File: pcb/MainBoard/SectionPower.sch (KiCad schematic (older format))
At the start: 14 parts, among them P3 Motor controller, P4 Motor battery, P5 Steering connector, P6 Arduino battery, SW1 OnOffDoubleSwitch

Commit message: PCB design finished
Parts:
- removed C_PWR_2, C_PWR_4: C, Capacitors_ThroughHole:C_Radial_D6.3_L11.2_P2.5, symbol C
- renumbered C_PWR_3 to C_PWR_2
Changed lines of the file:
@@
 NoConn ~ 3100 4000
 $Comp
-L GND #PWR044
+L GND #PWR042
 U 1 1 57FA5F2E
 P 5950 4950
-F 0 "#PWR044" H 5950 4700 50  0001 C CNN
+F 0 "#PWR042" H 5950 4700 50  0001 C CNN
 F 1 "GND" H 5950 4800 50  0000 C CNN
 F 2 "" H 5950 4950 50  0000 C CNN
@@
 MOTOR_B2
 $Comp
-L +5V #PWR045
+L +5V #PWR043
 U 1 1 57FA637B
 P 5950 4750
-F 0 "#PWR045" H 5950 4600 50  0001 C CNN
+F 0 "#PWR043" H 5950 4600 50  0001 C CNN
 F 1 "+5V" H 5950 4890 50  0000 C CNN
 F 2 "" H 5950 4750 50  0000 C CNN
@@
 $EndComp
 $Comp
-L C C_PWR_3
+L C C_PWR_2
 U 1 1 57FA6C6F
 P 3800 4800
-F 0 "C_PWR_3" H 3825 4900 50  0000 L CNN
+F 0 "C_PWR_2" H 3825 4900 50  0000 L CNN
 F 1 "C" H 3825 4700 50  0000 L CNN
 F 2 "Capacitors_ThroughHole:C_Radial_D6.3_L11.2_P2.5" H 3838 4650 50  0001 C CNN
@@
 	1    0    0    -1
 $EndComp
-$Comp
-L C C_PWR_4
-U 1 1 57FA6CEF
-P 4250 4800
-F 0 "C_PWR_4" H 4275 4900 50  0000 L CNN
-F 1 "C" H 4275 4700 50  0000 L CNN
-F 2 "Capacitors_ThroughHole:C_Radial_D6.3_L11.2_P2.5" H 4288 4650 50  0001 C CNN
-F 3 "" H 4250 4800 50  0000 C CNN
-	1    4250 4800
-	1    0    0    -1
-$EndComp
 Wire Wire Line
 	1900 4950 5050 4950
 Connection ~ 3800 4950
-Connection ~ 4250 4950
 Wire Wire Line
 	3500 4000 3500 4650
@@
 Wire Wire Line
 	5050 4650 5050 4750
-Connection ~ 4250 4650
-$Comp
-L C C_PWR_2
-U 1 1 57FA7057
-P 4200 2300
-F 0 "C_PWR_2" H 4225 2400 50  0000 L CNN
-F 1 "C" H 4225 2200 50  0000 L CNN
-F 2 "Capacitors_ThroughHole:C_Radial_D6.3_L11.2_P2.5" H 4238 2150 50  0001 C CNN
-F 3 "" H 4200 2300 50  0000 C CNN
-	1    4200 2300
-	1    0    0    -1
-$EndComp
 Wire Wire Line
 	3500 2150 5050 2150
 Connection ~ 3700 2150
-Connection ~ 4200 2150
 Wire Wire Line
 	1900 2450 5050 2450
@@
 Wire Wire Line
 	4650 2450 4650 3450
-Connection ~ 4200 2450
 Connection ~ 4650 2450
 Wire Wire Line

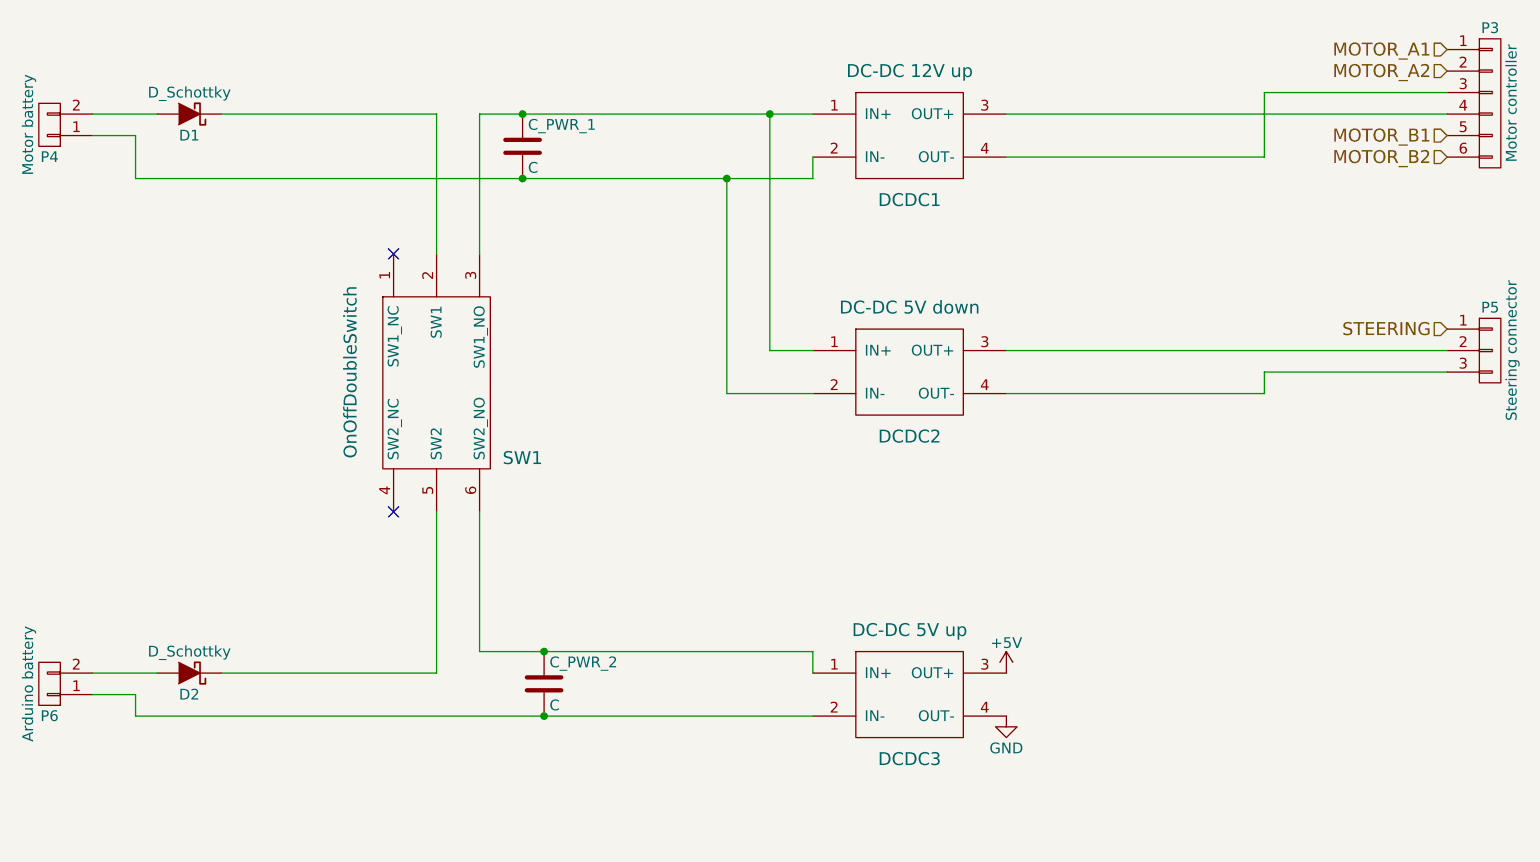
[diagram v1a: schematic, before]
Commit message: fixed power module ground connections
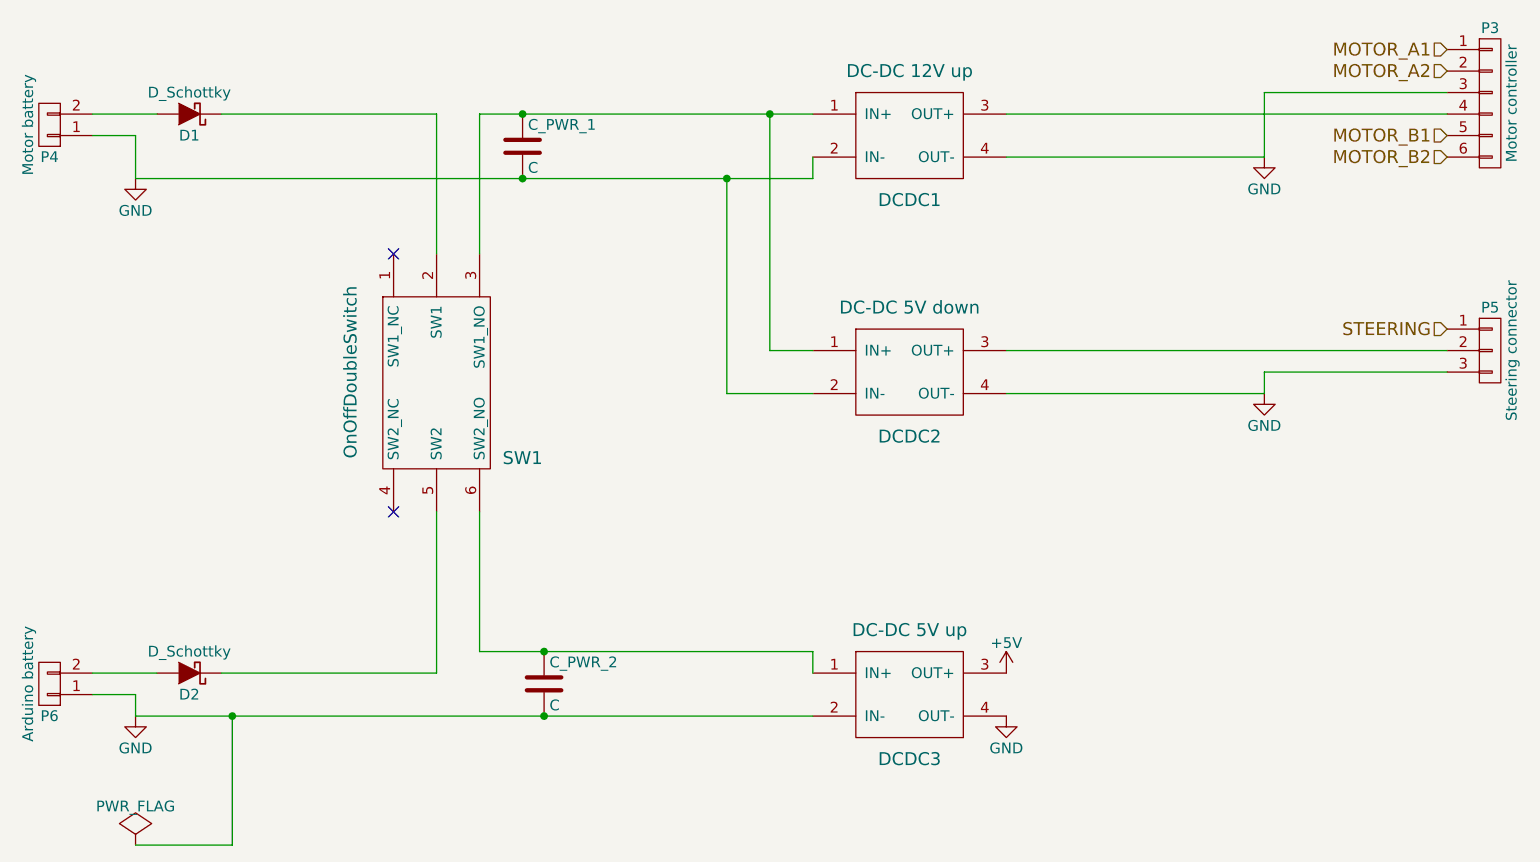
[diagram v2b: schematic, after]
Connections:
- net GND: now also C_PWR_1.2, C_PWR_2.2, DCDC1.2 (IN-), DCDC1.4 (OUT-), DCDC2.2 (IN-), DCDC2.4 (OUT-), DCDC3.2 (IN-), P3.3 (P3), P4.1 (P1), P5.3 (P3), P6.1 (P1)
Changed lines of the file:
@@
 	-1   0    0    1
 $EndComp
-Wire Wire Line
-	1700 2150 2000 2150
-Wire Wire Line
-	1700 4750 2000 4750
-Wire Wire Line
-	2300 4750 3300 4750
-Wire Wire Line
-	3300 4750 3300 4000
-Wire Wire Line
-	2300 2150 3300 2150
-Wire Wire Line
-	3300 2150 3300 2800
-Wire Wire Line
-	3500 2800 3500 2150
-Wire Wire Line
-	1900 2450 1900 2250
-Wire Wire Line
-	1900 2250 1700 2250
-Wire Wire Line
-	4650 3450 5050 3450
 NoConn ~ 3100 2800
-Wire Wire Line
-	5050 3250 4850 3250
-Wire Wire Line
-	1700 4850 1900 4850
-Wire Wire Line
-	1900 4850 1900 4950
 NoConn ~ 3100 4000
 $Comp
@@
 	1    0    0    -1
 $EndComp
-Wire Wire Line
-	5950 2150 8000 2150
-Wire Wire Line
-	8000 2050 7150 2050
 Text HLabel 8000 1850 0    60   Input ~ 0
 MOTOR_A1
@@
 	1    0    0    -1
 $EndComp
-Wire Wire Line
-	1900 4950 5050 4950
-Connection ~ 3800 4950
-Wire Wire Line
-	3500 4000 3500 4650
-Wire Wire Line
-	3500 4650 5050 4650
-Connection ~ 3800 4650
-Wire Wire Line
-	5050 4650 5050 4750
-Wire Wire Line
-	3500 2150 5050 2150
-Connection ~ 3700 2150
-Wire Wire Line
-	1900 2450 5050 2450
-Connection ~ 3700 2450
-Wire Wire Line
-	4650 2450 4650 3450
-Connection ~ 4650 2450
-Wire Wire Line
-	4850 3250 4850 2150
-Connection ~ 4850 2150
-Wire Wire Line
-	5050 2450 5050 2350
-Wire Wire Line
-	5950 2350 7150 2350
-Wire Wire Line
-	7150 2350 7150 2050
 $Comp
 L CONN_01X03 P5
@@
 	1    0    0    -1
 $EndComp
-Wire Wire Line
-	5950 3250 8000 3250
-Wire Wire Line
-	5950 3450 7150 3450
-Wire Wire Line
-	7150 3450 7150 3350
-Wire Wire Line
-	7150 3350 8000 3350
 Text HLabel 8000 3150 0    60   Input ~ 0
 STEERING
+Wire Wire Line
+	1700 2150 2000 2150
+Wire Wire Line
+	1700 4750 2000 4750
+Wire Wire Line
+	2300 4750 3300 4750
+Wire Wire Line
+	3300 4750 3300 4000
+Wire Wire Line
+	2300 2150 3300 2150
+Wire Wire Line
+	3300 2150 3300 2800
+Wire Wire Line
+	3500 2800 3500 2150
+Wire Wire Line
+	1900 2450 1900 2250
+Wire Wire Line
+	1900 2250 1700 2250
+Wire Wire Line
+	4650 3450 5050 3450
+Wire Wire Line
+	5050 3250 4850 3250
+Wire Wire Line
+	1700 4850 1900 4850
+Wire Wire Line
+	1900 4850 1900 4950
+Wire Wire Line
+	5950 2150 8000 2150
+Wire Wire Line
+	8000 2050 7150 2050
+Wire Wire Line
+	1900 4950 5050 4950
+Connection ~ 3800 4950
+Wire Wire Line
+	3500 4000 3500 4650
+Wire Wire Line
+	3500 4650 5050 4650
+Connection ~ 3800 4650
+Wire Wire Line
+	5050 4650 5050 4750
+Wire Wire Line
+	3500 2150 5050 2150
+Connection ~ 3700 2150
+Wire Wire Line
+	1900 2450 5050 2450
+Connection ~ 3700 2450
+Wire Wire Line
+	4650 2450 4650 3450
+Connection ~ 4650 2450
+Wire Wire Line
+	4850 3250 4850 2150
+Connection ~ 4850 2150
+Wire Wire Line
+	5050 2450 5050 2350
+Wire Wire Line
+	5950 2350 7150 2350
+Wire Wire Line
+	7150 2350 7150 2050
+Wire Wire Line
+	5950 3250 8000 3250
+Wire Wire Line
+	5950 3450 7150 3450
+Wire Wire Line
+	7150 3450 7150 3350
+Wire Wire Line
+	7150 3350 8000 3350
+$Comp
+L GND #PWR044
+U 1 1 581E19B8
+P 7150 2350
+F 0 "#PWR044" H 7150 2100 50  0001 C CNN
+F 1 "GND" H 7150 2200 50  0000 C CNN
+F 2 "" H 7150 2350 50  0000 C CNN
+F 3 "" H 7150 2350 50  0000 C CNN
+	1    7150 2350
+	1    0    0    -1
+$EndComp
+$Comp
+L GND #PWR045
+U 1 1 581E1B0F
+P 7150 3450
+F 0 "#PWR045" H 7150 3200 50  0001 C CNN
+F 1 "GND" H 7150 3300 50  0000 C CNN
+F 2 "" H 7150 3450 50  0000 C CNN
+F 3 "" H 7150 3450 50  0000 C CNN
+	1    7150 3450
+	1    0    0    -1
+$EndComp
+$Comp
+L GND #PWR046
+U 1 1 581E2085
+P 1900 4950
+F 0 "#PWR046" H 1900 4700 50  0001 C CNN
+F 1 "GND" H 1900 4800 50  0000 C CNN
+F 2 "" H 1900 4950 50  0000 C CNN
+F 3 "" H 1900 4950 50  0000 C CNN
+	1    1900 4950
+	1    0    0    -1
+$EndComp
+$Comp
+L GND #PWR047
+U 1 1 581E20B4
+P 1900 2450
+F 0 "#PWR047" H 1900 2200 50  0001 C CNN
+F 1 "GND" H 1900 2300 50  0000 C CNN
+F 2 "" H 1900 2450 50  0000 C CNN
+F 3 "" H 1900 2450 50  0000 C CNN
+	1    1900 2450
+	1    0    0    -1
+$EndComp
+$Comp
+L PWR_FLAG #FLG048
+U 1 1 581E27A6
+P 1900 5550
+F 0 "#FLG048" H 1900 5645 50  0001 C CNN
+F 1 "PWR_FLAG" H 1900 5730 50  0000 C CNN
+F 2 "" H 1900 5550 50  0000 C CNN
+F 3 "" H 1900 5550 50  0000 C CNN
+	1    1900 5550
+	1    0    0    -1
+$EndComp
+Wire Wire Line
+	1900 5550 2350 5550
+Wire Wire Line
+	2350 5550 2350 4950
+Connection ~ 2350 4950
 $EndSCHEMATC
